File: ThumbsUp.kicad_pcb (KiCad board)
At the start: 2 copper layers, 401.4 x 336.1 mm, 169 parts, among them IC1 RP2040, IC2 W25Q128JVSIM, J1 Conn_01x04_Male, J10 Raiser_Male, J11 Raiser_Female, J12 Raiser_Male, J13 Raiser_Female, J14 Raiser_Male, J15 Raiser_Female, J16 Raiser_Male, J17 Raiser_Female, J18 Raiser_Male, J19 52559-1233, J2 Conn_01x04_Male, J20 Conn_01x04_Female, J21 Conn_01x04_Female, J22 Conn_01x04_Female, J23 Conn_01x04_Female, J24 Conn_01x04_Male, J25 Conn_01x04_Male, J26 Conn_01x04_Male, J27 Conn_01x04_Male, J28 Conn_01x04_Female, J29 Conn_01x04_Female, J3 Conn_01x04_Female, J30 Conn_01x04_Female, J31 Conn_01x04_Female, J32 USB_C_Receptacle_USB2.0, J4 Conn_01x04_Male, J5 Conn_01x04_Female, J6 Conn_01x04_Male, J7 Conn_01x04_Male, J8 Conn_01x04_Male, J9 Raiser_Female, U1 NCP1117-3.3_SOT223, Y1 ABLS-12.000MHZ-B4-T

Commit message: ThumbsUp! v10 moved the keys around
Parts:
- moved MX44 3.58 mm to (258.0, 296.5)
- moved MX11 3.58 mm to (99.0, 279.3)
- moved MX12 3.58 mm to (92.4, 295.6)
- moved MX13 3.58 mm to (85.9, 311.8)
- moved MX32 3.58 mm to (197.7, 295.5)
- moved MX35 3.58 mm to (210.2, 277.0)
- moved MX36 3.58 mm to (216.8, 293.2)
- moved MX37 3.58 mm to (223.3, 309.5)
- moved MX39 3.58 mm to (229.2, 274.7)
- moved MX4 3.58 mm to (60.9, 274.7)
- moved MX41 3.58 mm to (242.3, 307.2)
- moved MX42 3.58 mm to (244.9, 264.1)
- moved MX43 3.58 mm to (251.4, 280.3)
- moved MX3 3.58 mm to (32.1, 296.6)
- moved MX1 3.58 mm to (45.3, 264.1)
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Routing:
- net COL4: track 206.9 -> 64.6 mm
- net COL7: track 212.6 -> 82.5 mm, vias 2 -> 1
- net COL5: track 163.2 -> 70.5 mm
- net COL3: track 123.8 -> 51.6 mm
- net COL6: track 173.7 -> 105.8 mm, vias 4 -> 2
- net COL2: track 116.4 -> 51.1 mm, vias 2 -> 1
- net Net-(D16-Pad2): track 64.6 -> 0.00 mm, vias 1 -> 0
- net COL8: track 140.0 -> 79.7 mm
- net Net-(D14-Pad2): track 64.8 -> 6.29 mm, vias 2 -> 1
- net COL0: track 105.8 -> 50.0 mm
- net Net-(D15-Pad2): track 65.0 -> 9.72 mm
- net COL1: track 105.7 -> 50.5 mm
- net Net-(D26-Pad2): track 66.6 -> 13.4 mm
- net Net-(D5-Pad2): track 52.4 -> 0.00 mm, vias 1 -> 0
- net Net-(D6-Pad2): track 51.2 -> 0.00 mm, vias 1 -> 0
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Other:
- board size 401.4 x 336.1 mm -> 400 x 336.1 mm
- board text added: "Thumbs Up! v10 by Sasha Karmanov April 02, 2024 https://github.com/ak66666/ThumbsUpV10"
- board text removed: "Thumbs Up! by Sasha Karmanov October 28, 2022 https://github.com/ak66666/ThumbsUpUnsplitV2Rp2040"

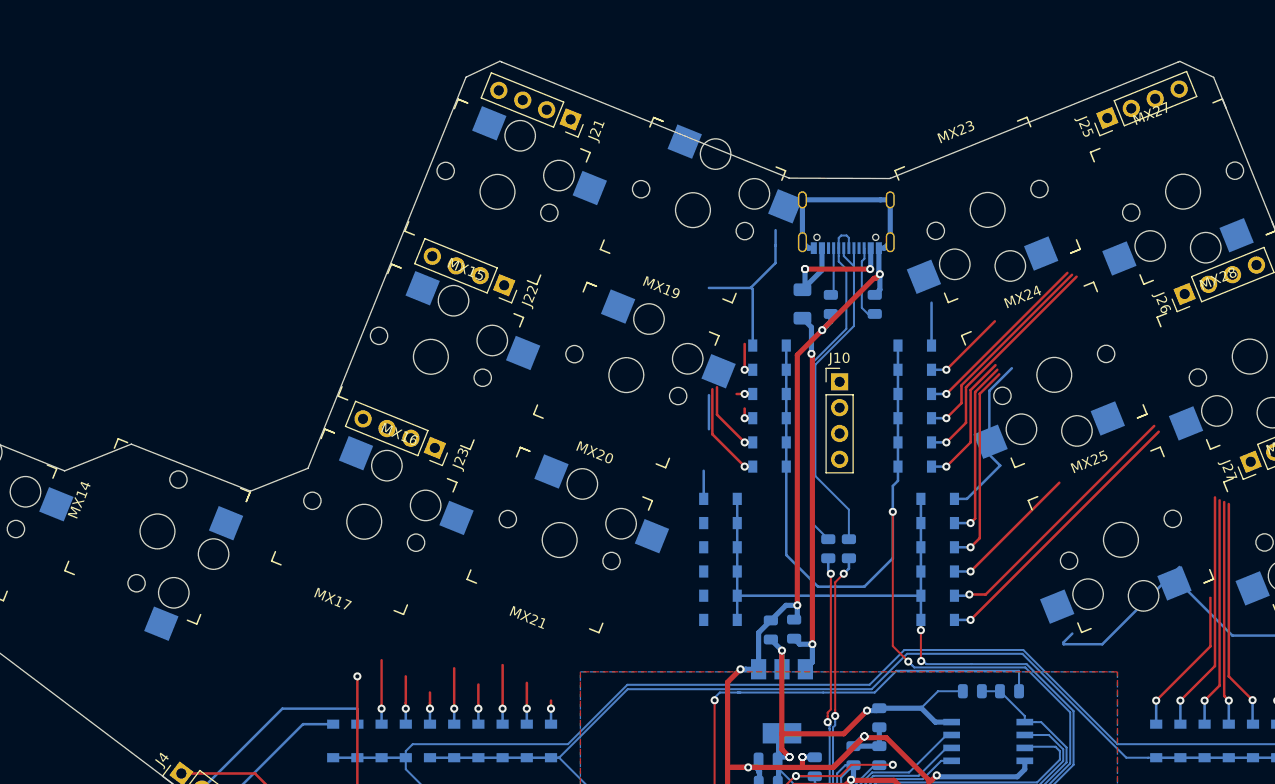
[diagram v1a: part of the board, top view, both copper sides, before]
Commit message: Redefined boundaries of the middle PCB.
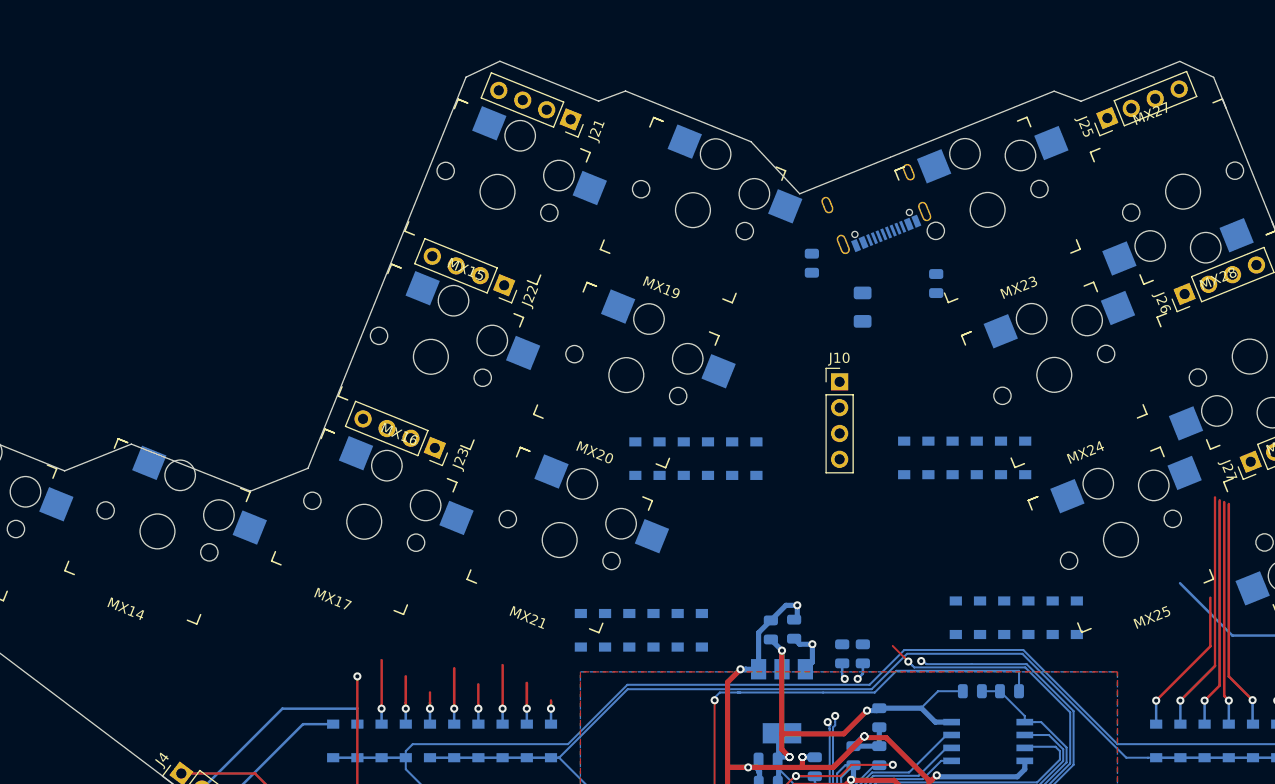
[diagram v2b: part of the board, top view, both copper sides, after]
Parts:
- moved D16 13.8 mm to (121.2, 197.1), turned to 90 degrees
- moved D27 13.7 mm to (170.0, 195.8), turned to 90 degrees
- moved D15 13.2 mm to (126.6, 180.2), turned to 90 degrees
- moved D21 13.1 mm to (133.1, 197.1), turned to 90 degrees
- moved D5 11.9 mm to (123.6, 197.1), turned to 90 degrees
- moved D24 11.8 mm to (158.1, 195.8), turned to 90 degrees
- moved D35 11.5 mm to (167.6, 195.8), turned to 90 degrees
- moved D8 11.4 mm to (130.7, 197.1), turned to 90 degrees
- moved D20 11.2 mm to (138.5, 180.2), turned to 90 degrees
- moved D23 11.1 mm to (153.0, 180.1), turned to 90 degrees
- moved D1 10.9 mm to (128.9, 180.2), turned to 90 degrees
- moved D26 10.9 mm to (164.9, 180.1), turned to 90 degrees
- moved D6 10.7 mm to (126.0, 197.1), turned to 90 degrees
- moved D7 10.5 mm to (128.3, 197.1), turned to 90 degrees
- moved R1 10.4 mm to (146.9, 199.4)
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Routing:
- net ROW0: track 114.6 -> 46.5 mm, vias 2 -> 1
- net GND: track 423.0 -> 360.4 mm, vias 23 -> 21
- net ROW1: track 90.0 -> 44.1 mm, vias 2 -> 1
- net D-: track 34.2 -> 0.00 mm
- net D+: track 33.8 -> 0.00 mm
- net +5V: track 37.2 -> 4.77 mm, vias 2 -> 1
- net Net-(D27-Pad2): track 27.8 -> 0.00 mm, vias 1 -> 0
- net Net-(D35-Pad2): track 26.6 -> 0.00 mm, vias 1 -> 0
- net Net-(D31-Pad2): track 23.1 -> 0.00 mm, vias 1 -> 0
- net Net-(D32-Pad2): track 20.7 -> 0.00 mm, vias 1 -> 0
- net Net-(D37-Pad2): track 19.8 -> 0.00 mm, vias 1 -> 0
- net Net-(D33-Pad2): track 18.3 -> 0.00 mm, vias 1 -> 0
- net Net-(D38-Pad2): track 17.8 -> 0.00 mm, vias 1 -> 0
- net Net-(D24-Pad2): track 16.8 -> 0.00 mm
- net Net-(D20-Pad2): track 16.6 -> 0.00 mm
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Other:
- outline, holes or cut-outs redrawn
